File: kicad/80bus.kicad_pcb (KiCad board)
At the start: 2 copper layers, 145 x 130 mm, 70 parts, among them M1 MountingHole_3.2mm_M3_Pad, M2 MountingHole_3.2mm_M3_Pad, M3 MountingHole_3.2mm_M3_Pad, M4 MountingHole_3.2mm_M3_Pad, SW1 SW_SPST, T1 10uF, T2 10uF, U1 4049, U2 TL497_Fixed, U3 LM78L12_TO92, U4 4040, U5 LMC7660

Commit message: Silkscreen tidy
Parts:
- R2: value 680 -> 1K
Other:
- board text added: "6dd64576-4be6-4520-a357-94d72388fa75"
- board text added: "Version 2.3"
- board text removed: "2f09e51e-ebb1-4036-8dc7-cbf1092a799f"
- board text removed: "Version 2.2"
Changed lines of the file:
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@@
   (title_block
     (title "Nascom 2708 / 2716 EPROM programmer")
-    (date "2023-05-21")
-    (rev "2.1")
+    (date "2023-06-21")
+    (rev "2.3")
   )
   (layers
@@
         (effects (font (size 1 1) (thickness 0.15)))
     )
-    (fp_text value "680" (at 15.7734 0.0508) (layer "F.SilkS")
+    (fp_text value "1K" (at 15.7734 0.0508) (layer "F.SilkS")
         (effects (font (size 1 1) (thickness 0.15)))
     )
@@
   (gr_line (start 220.345 77.3176) (end 148.4376 77.3684)
     (stroke (width 0.12) (type default)) (layer "F.SilkS"))
-  (gr_line (start 258.3942 121.4628) (end 258.400852 115.669763)
+  (gr_line (start 257.472446 121.480869) (end 257.470713 115.665387)
     (stroke (width 0.12) (type default)) (layer "F.SilkS"))
   (gr_line (start 220.9038 77.3176) (end 222.150149 77.317978)
     (stroke (width 0.12) (type default)) (layer "F.SilkS"))
-  (gr_line (start 270.8656 109.982) (end 270.8656 85.2932)
+  (gr_line (start 270.8656 109.982) (end 270.863784 86.161088)
     (stroke (width 0.12) (type default)) (layer "F.SilkS"))
-  (gr_line (start 258.400852 115.669763) (end 270.890413 115.669763)
+  (gr_line (start 257.470713 115.665387) (end 270.890413 115.669763)
     (stroke (width 0.12) (type default)) (layer "F.SilkS"))
   (gr_rect (start 171.172735 127.903285) (end 198.043076 157.078709)
@@
     (pts
       (xy 260.898167 126.278685)
-      (xy 258.95907 126.278685)
+      (xy 258.976537 126.278241)
       (xy 258.971586 116.573677)
       (xy 273.867491 116.551824)
@@
   (gr_line (start 214.665167 96.234005) (end 222.150996 96.230094)
     (stroke (width 0.12) (type default)) (layer "F.SilkS"))
-  (gr_line (start 260.9596 85.2932) (end 270.8656 85.2932)
+  (gr_line (start 260.966518 86.161494) (end 270.863784 86.161088)
     (stroke (width 0.12) (type default)) (layer "F.SilkS"))
-  (gr_line (start 215.773 121.4882) (end 258.3942 121.4628)
+  (gr_line (start 217.428511 121.477668) (end 257.472446 121.480869)
     (stroke (width 0.12) (type default)) (layer "F.SilkS"))
   (gr_line (start 148.4376 77.3684) (end 148.4376 105.3592)
@@
   (gr_line (start 217.423733 99.585103) (end 217.428511 121.477668)
     (stroke (width 0.12) (type default)) (layer "F.SilkS"))
-  (gr_line (start 260.9596 77.343) (end 260.9596 85.2932)
+  (gr_line (start 260.9596 77.343) (end 260.966518 86.161494)
     (stroke (width 0.12) (type default)) (layer "F.SilkS"))
   (gr_line (start 214.6554 105.3592) (end 214.665167 96.234005)
@@
     (effects (font (size 1.5 1.5) (thickness 0.3) bold) (justify left bottom))
   )
-  (gr_text "2f09e51e-ebb1-4036-8dc7-cbf1092a799f" (at 214.239431 203.176185) (layer "F.SilkS")
+  (gr_text "6dd64576-4be6-4520-a357-94d72388fa75" (at 214.239431 203.176185) (layer "F.SilkS")
     (effects (font (size 0.8 0.8) (thickness 0.15)))
   )
@@
     (effects (font (size 1.5 1.5) (thickness 0.3) bold) (justify left bottom))
   )
-  (gr_text "Version 2.2" (at 150.954796 201.092783) (layer "F.SilkS")
+  (gr_text "Version 2.3" (at 150.954796 201.092783) (layer "F.SilkS")
     (effects (font (size 1 1) (thickness 0.15)))
   )
@@
   (segment (start 206.751776 132.159351) (end 202.593551 132.159351) (width 0.5) (layer "F.Cu") (net 14))
   (via (at 206.751776 132.159351) (size 0.8) (drill 0.4) (layers "F.Cu" "B.Cu") (net 14))
+  (segment (start 215.586161 110.168839) (end 206.733537 119.021463) (width 0.5) (layer "B.Cu") (net 14))
   (segment (start 217.464 80.4672) (end 217.464 85.3078) (width 1) (layer "B.Cu") (net 14))
   (segment (start 217.5002 85.344) (end 217.5002 91.2368) (width 1) (layer "B.Cu") (net 14))
-  (segment (start 213.995 111.76) (end 206.733537 119.021463) (width 0.5) (layer "B.Cu") (net 14))
+  (segment (start 217.5002 91.2368) (end 215.586161 93.150839) (width 0.5) (layer "B.Cu") (net 14))
   (segment (start 206.733537 132.141112) (end 206.751776 132.159351) (width 0.5) (layer "B.Cu") (net 14))
   (segment (start 206.751776 132.159351) (end 206.733537 132.150232) (width 0.5) (layer "B.Cu") (net 14))
+  (segment (start 215.586161 93.150839) (end 215.586161 110.168839) (width 0.5) (layer "B.Cu") (net 14))
   (segment (start 206.733537 119.021463) (end 206.733537 132.141112) (width 0.5) (layer "B.Cu") (net 14))
-  (segment (start 213.995 94.742) (end 213.995 111.76) (width 0.5) (layer "B.Cu") (net 14))
-  (segment (start 217.5002 91.2368) (end 213.995 94.742) (width 0.5) (layer "B.Cu") (net 14))
   (segment (start 191.5922 174.371) (end 192.5066 175.2854) (width 0.25) (layer "F.Cu") (net 15))
   (segment (start 201.0664 175.2854) (end 202.3872 176.6062) (width 0.25) (layer "F.Cu") (net 15))

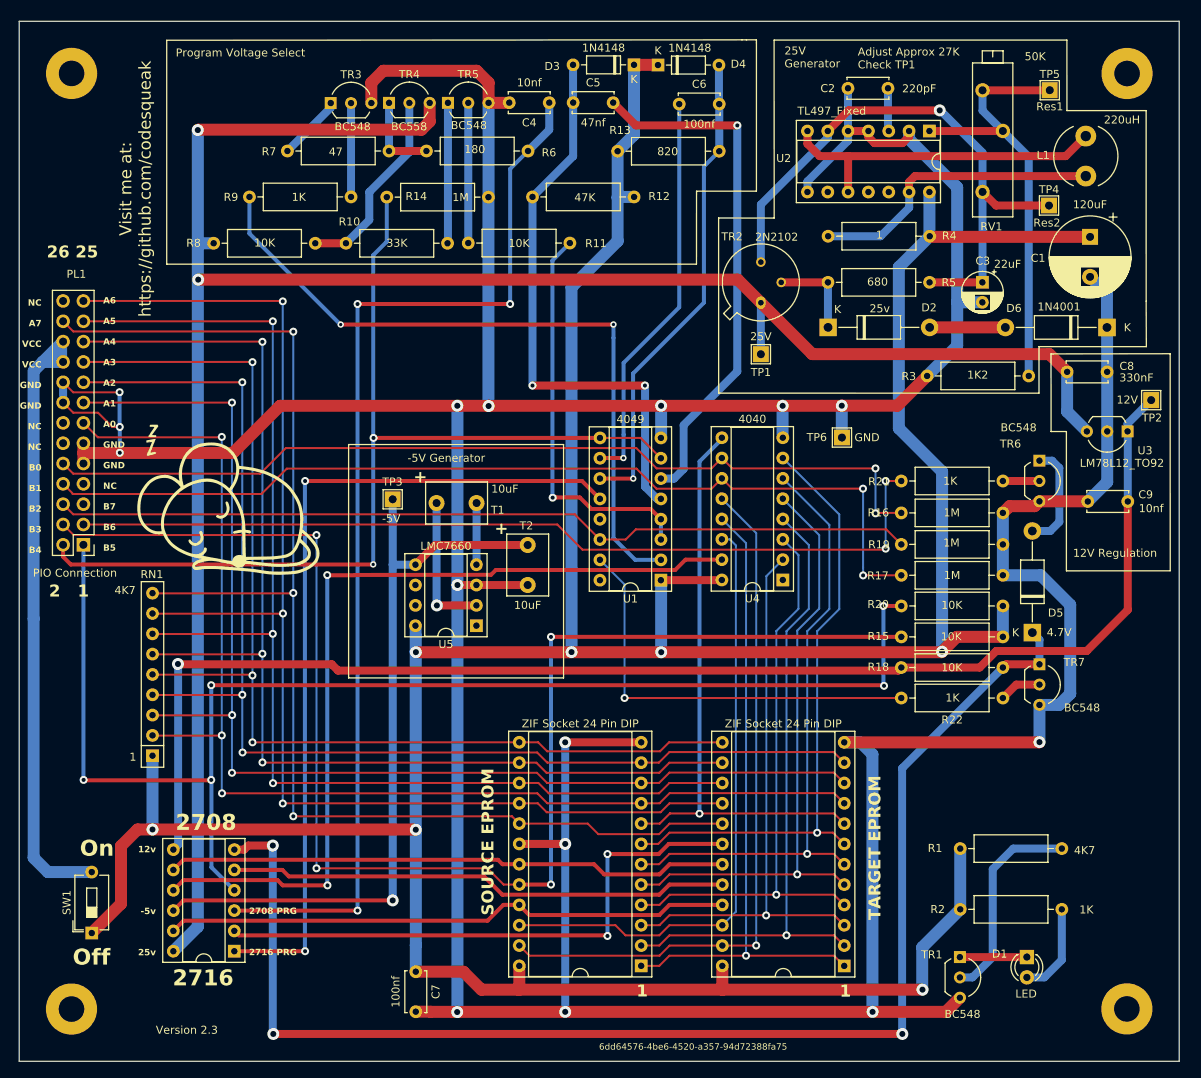
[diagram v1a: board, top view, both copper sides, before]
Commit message: Add aux power feeds
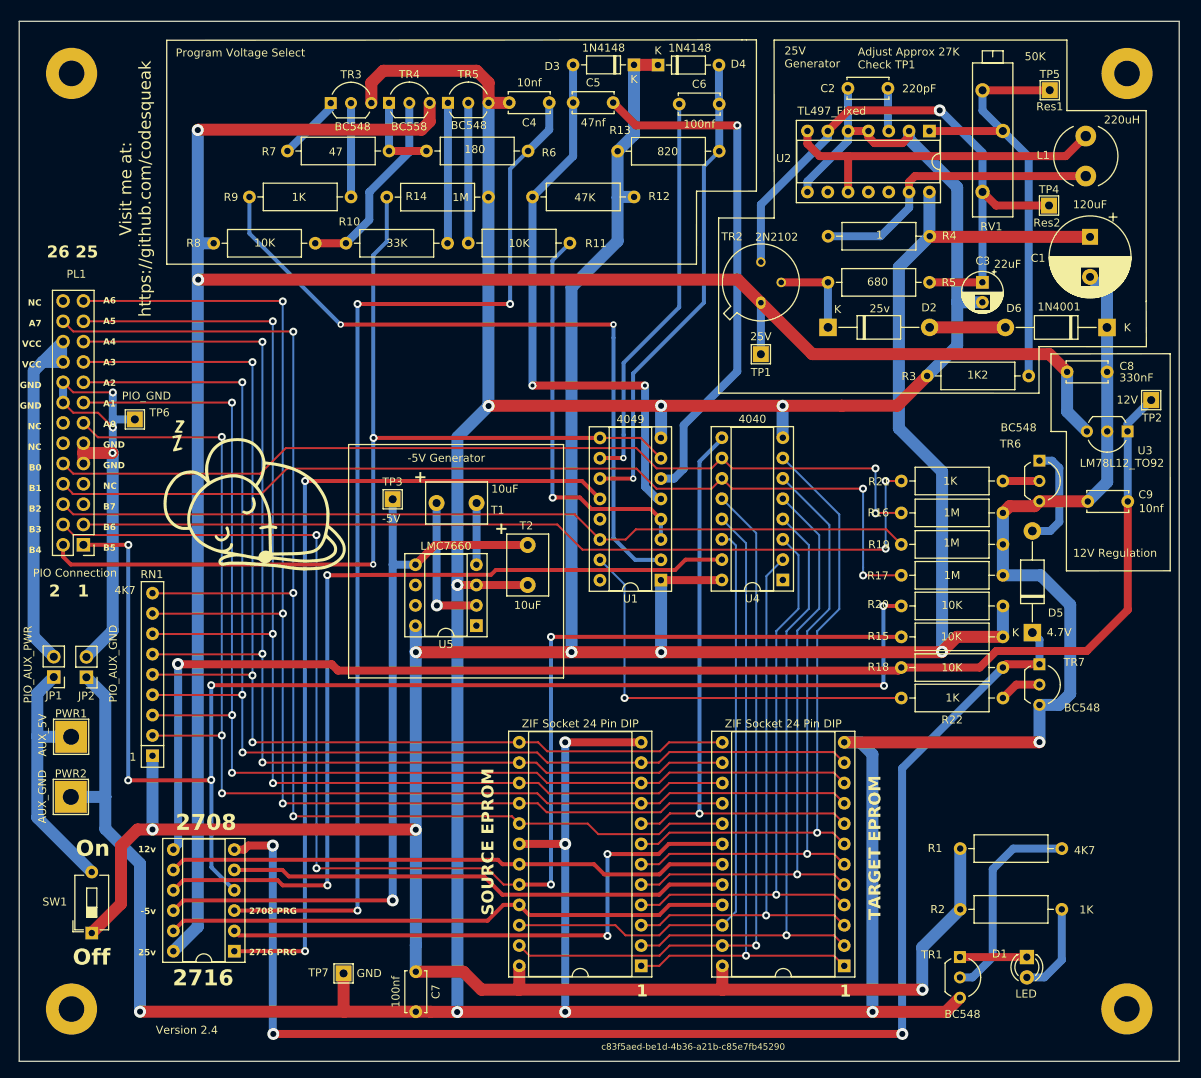
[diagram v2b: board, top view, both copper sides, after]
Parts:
- added JP1: PIO_AUX_PWR, Connector_PinHeader_2.54mm:PinHeader_1x02_P2.54mm_Vertical, F.Cu at (134.3, 157.0)
- added JP2: PIO_AUX_GND, Connector_PinHeader_2.54mm:PinHeader_1x02_P2.54mm_Vertical, F.Cu at (138.4, 157.0)
- added PWR1: AUX_5V, TestPoint:TestPoint_THTPad_4.0x4.0mm_Drill2.0mm, F.Cu at (136.5, 164.4)
- added PWR2: AUX_GND, TestPoint:TestPoint_THTPad_4.0x4.0mm_Drill2.0mm, F.Cu at (136.5, 171.9)
- added TP7: GND, TestPoint:TestPoint_THTPad_2.0x2.0mm_Drill1.0mm, F.Cu at (170.5, 194.0)
- TP6: value GND -> PIO_GND
- moved TP6 88.4 mm to (144.5, 124.8)
- moved G1 3.32 mm to (158.8, 134.9)
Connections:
- PL1 pad 11: GND -> PIO_GND
- PL1 pad 16: GND -> PIO_GND
- PL1 pad 18: GND -> PIO_GND
- PL1 pad 9: GND -> PIO_GND
- SW1 pad 2: VCC -> Net-(JP1-A)
- TP6 pad 1: GND -> PIO_GND
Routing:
- net PIO_GND: track 0.00 -> 60.0 mm, vias 0 -> 3
- net Net-(JP1-A): track 0.00 -> 32.3 mm
- net VCC: track 83.1 -> 51.1 mm
- net GND: track 615.8 -> 620.1 mm, vias 15 -> 11
- net B5: track 168.6 -> 168.7 mm, vias 5 -> 6
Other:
- board text added: "Version 2.4"
- board text added: "c83f5aed-be1d-4b36-a21b-c85e7fb45290"
- board text removed: "6dd64576-4be6-4520-a357-94d72388fa75"
- board text removed: "Version 2.3"

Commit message: Add soft start
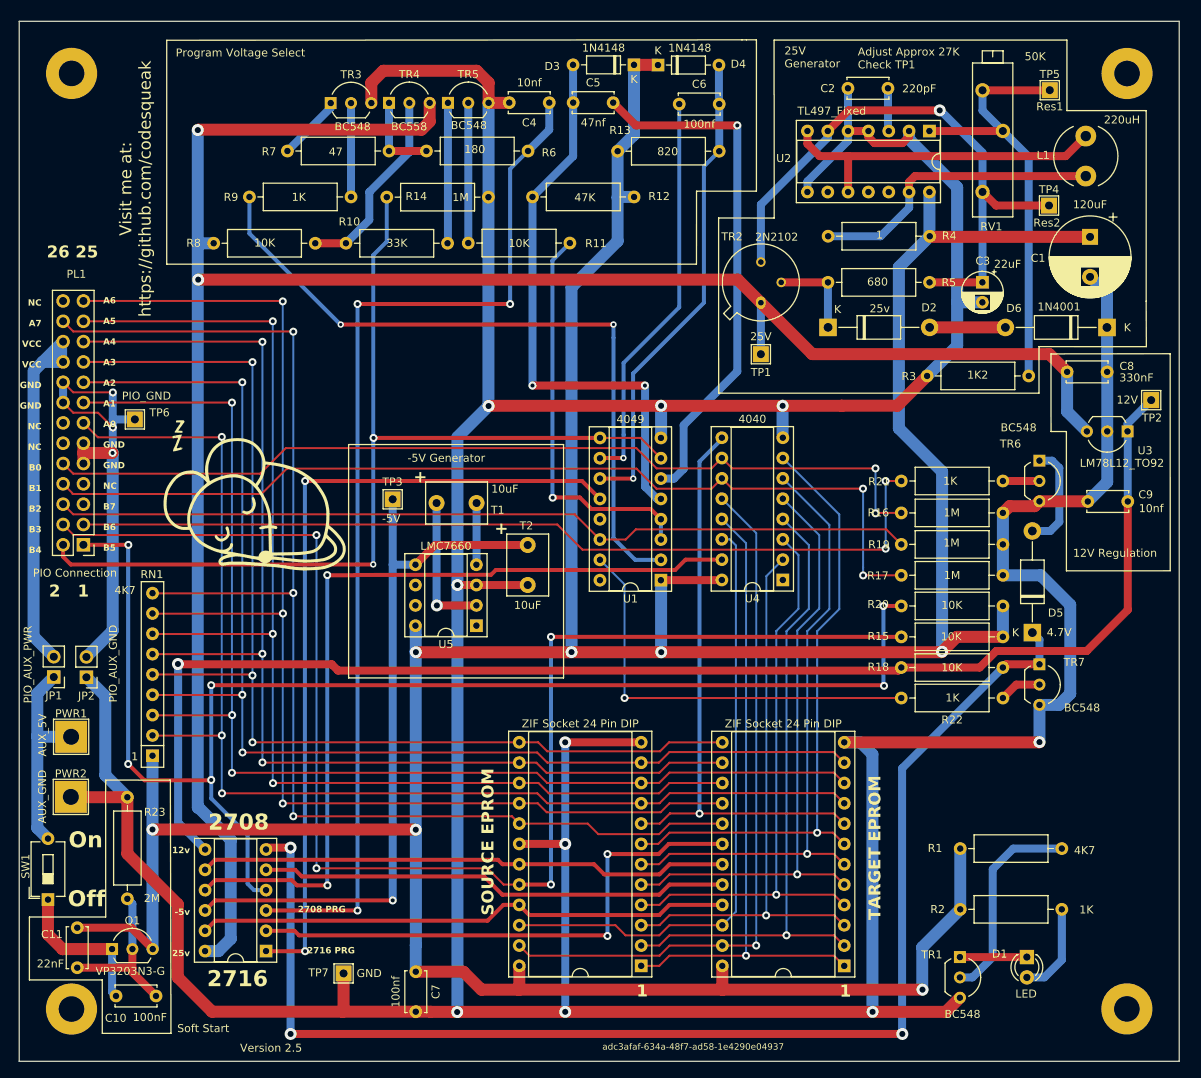
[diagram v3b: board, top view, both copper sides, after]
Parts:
- added C10: 100nF, Capacitor_THT:C_Disc_D5.0mm_W2.5mm_P5.00mm, F.Cu at (142.1, 196.8)
- added C11: 22nF, Capacitor_THT:C_Disc_D5.0mm_W2.5mm_P5.00mm, F.Cu at (137.2, 188.3)
- added Q1: VP3203N3-G, Package_TO_SOT_THT:TO-92L_Inline_Wide, F.Cu at (141.6, 191.0)
- added R23: 2M, Resistor_THT:R_Axial_DIN0309_L9.0mm_D3.2mm_P12.70mm_Horizontal, F.Cu at (143.5, 184.7)
- moved SW1 6.88 mm to (133.6, 184.8)
- moved SW_2708_2716_1 3.97 mm to (160.9, 191.2)
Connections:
- SW1 pad 1: SWITCHED 5V -> Net-(Q1-S)
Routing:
- net Net-(Q1-G): track 0.00 -> 20.6 mm
- net Net-(Q1-S): track 0.00 -> 19.2 mm
- net SWITCHED 5V: track 450.0 -> 458.3 mm
- net Net-(JP1-A): track 32.3 -> 25.9 mm
- net 2716_PRG_PWR: track 105.4 -> 101.4 mm
- net GENERATED -5V: track 96.0 -> 92.0 mm
- net Net-(SKT1-ZIF-Donor_1-Pin_21): track 71.0 -> 67.0 mm
- net Net-(SW_2708_2716_1-Pin_9): track 109.0 -> 105.0 mm
- net Net-(SKT1-ZIF-Donor_1-Pin_19): track 70.4 -> 66.5 mm
- net 2708_PRG_PWR: track 137.5 -> 133.5 mm
- net Net-(SKT2-ZIF-Target_1-Pin_20): track 62.8 -> 58.8 mm
- net Net-(SKT2-ZIF-Target_1-Pin_18): track 72.0 -> 68.0 mm
- net Net-(D5-K): track 166.5 -> 162.6 mm
- net GENERATED 25V: track 265.9 -> 268.7 mm
- net GND: track 620.1 -> 617.6 mm, vias 11 -> 10
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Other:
- board text added: "Soft Start"
- board text added: "Version 2.5"
- board text added: "adc3afaf-634a-48f7-ad58-1e4290e04937"
- board text removed: "Version 2.4"
- board text removed: "c83f5aed-be1d-4b36-a21b-c85e7fb45290"

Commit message: Minor error - wrong resistor value as R13
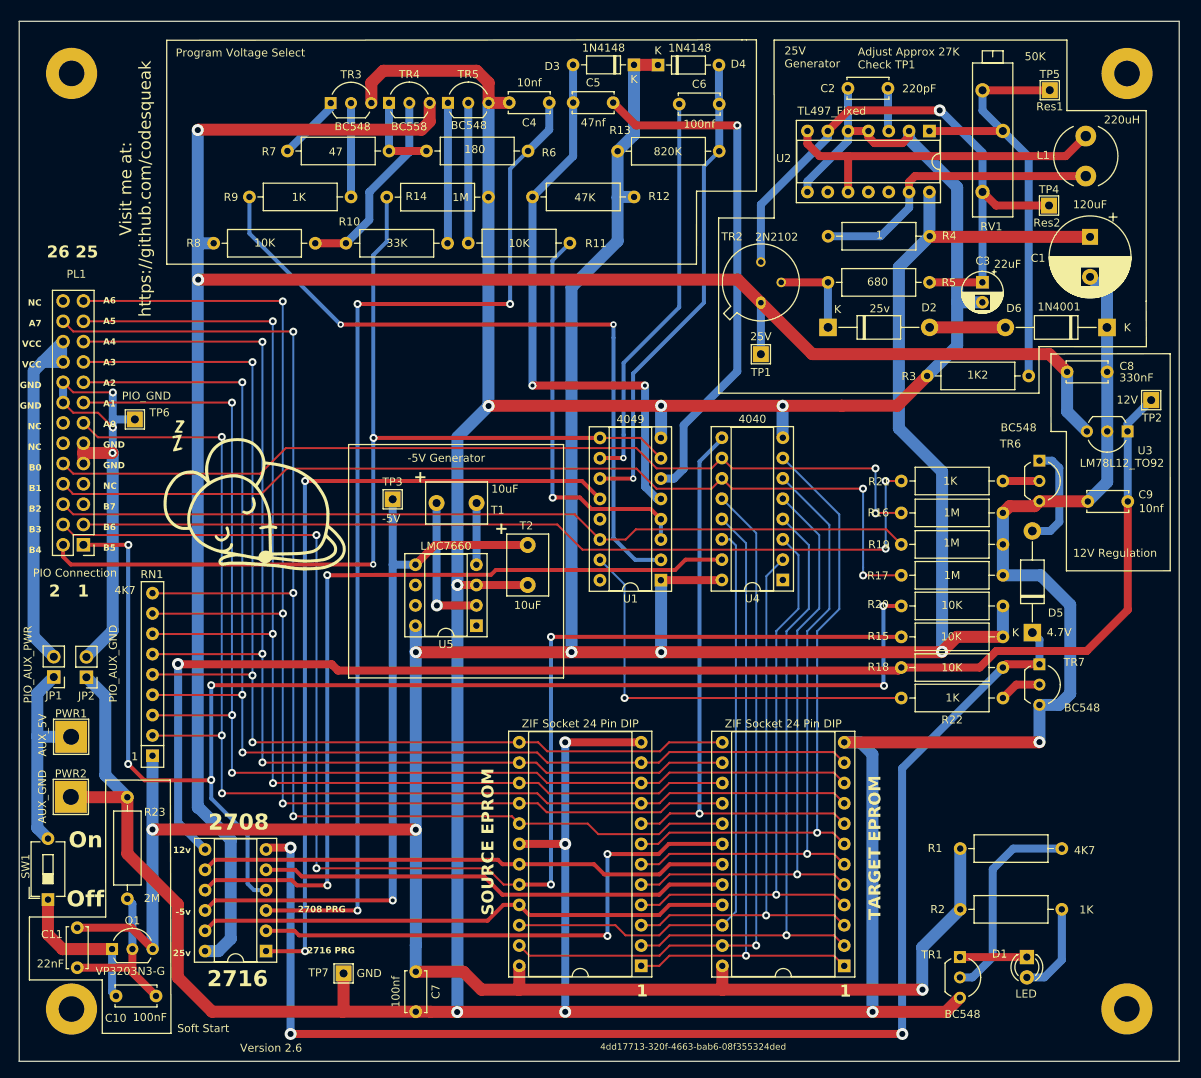
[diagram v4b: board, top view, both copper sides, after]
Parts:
- R13: value 820 -> 820K
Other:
- board text added: "4dd17713-320f-4663-bab6-08f355324ded"
- board text added: "Version 2.6"
- board text removed: "Version 2.5"
- board text removed: "adc3afaf-634a-48f7-ad58-1e4290e04937"
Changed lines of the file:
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@@
   (title_block
     (title "Nascom 2708 / 2716 EPROM programmer")
-    (date "2023-08-14")
-    (rev "2.5")
+    (date "2023-09-01")
+    (rev "2.6")
   )
   (layers
@@
         (effects (font (size 1 1) (thickness 0.15)))
     )
-    (fp_text value "820" (at 6.258372 0.041469) (layer "F.SilkS")
+    (fp_text value "820K" (at 6.258372 0.041469) (layer "F.SilkS")
         (effects (font (size 1 1) (thickness 0.15)))
     )
@@
     (effects (font (size 1.5 1.5) (thickness 0.3) bold) (justify left bottom))
   )
-  (gr_text "adc3afaf-634a-48f7-ad58-1e4290e04937" (at 214.239431 203.176185) (layer "F.SilkS")
+  (gr_text "4dd17713-320f-4663-bab6-08f355324ded" (at 214.239431 203.176185) (layer "F.SilkS")
     (effects (font (size 0.8 0.8) (thickness 0.15)))
   )
@@
     (effects (font (size 1.5 1.5) (thickness 0.3) bold) (justify left bottom))
   )
-  (gr_text "Version 2.5" (at 161.482753 203.335799) (layer "F.SilkS")
+  (gr_text "Version 2.6" (at 161.482753 203.335799) (layer "F.SilkS")
     (effects (font (size 1 1) (thickness 0.15)))
   )
@@
     (effects (font (size 1 1) (thickness 0.15)) (justify left bottom))
   )
-  (gr_text "12v\n\n\n\n\n\n-5v\n\n\n\n25v\n\n" (at 151.347081 193.244902) (layer "F.SilkS")
+  (gr_text "12v\n\n\n\n\n\n-5v\n\n\n\n25v\n\n" (at 151.457273 193.232889) (layer "F.SilkS")
     (effects (font (size 0.8 0.8) (thickness 0.2) bold) (justify right bottom))
   )
@@
     (effects (font (size 2 2) (thickness 0.5) bold) (justify left bottom))
   )
-  (gr_text "Off" (at 136.058612 185.858247) (layer "F.SilkS")
+  (gr_text "Off" (at 135.903224 185.879132) (layer "F.SilkS")
     (effects (font (size 2 2) (thickness 0.5) bold) (justify left bottom))
   )

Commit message: Update docs
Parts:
- removed M1, M2, M3, M4: MountingHole_3.2mm_M3_Pad, MountingHole:MountingHole_3.2mm_M3_Pad
- added G001: LOGO, 80bus:qr-code, B.Cu at (140.8, 88.4)
- D6: footprint Diode_THT:D_DO-41_SOD81_P12.70mm_Horizontal -> Diode_THT:D_DO-41_SOD81_P10.16mm_Horizontal
- Q1: footprint Package_TO_SOT_THT:TO-92L_Inline_Wide -> Package_TO_SOT_THT:TO-92L_Inline
- SW1: value SW_SPST -> SW_SPDT; footprint Button_Switch_THT:SW_DIP_SPSTx01_Slide_6.7x4.1mm_W7.62mm_P2.54mm_LowProfile -> Connector_PinHeader_2.54mm:PinHeader_1x03_P2.54mm_Vertical
- TR1, TR3, TR4, TR5, TR6, TR7, U3: footprint Package_TO_SOT_THT:TO-92_Inline_Wide -> Package_TO_SOT_THT:TO-92_Inline
- moved SW1 6.85 mm to (136.5, 178.6), turned to 0 degrees
- moved TR4 2.69 mm to (178.8, 84.5), turned to 180 degrees
- moved D5 0.90 mm to (257.5, 151.4)
- moved R23 0.66 mm to (142.9, 184.6)
- moved C10 0.51 mm to (141.6, 196.8)
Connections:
- SW1 pad 1: Net-(Q1-S) -> unconnected-(SW1-A-Pad1)
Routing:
- net GND: track 617.6 -> 630.3 mm
- net Net-(JP1-A): track 25.9 -> 32.2 mm
- net GENERATED 25V: track 268.7 -> 264.8 mm
- net Net-(D2-A): track 9.46 -> 12.0 mm
- net Net-(TR5-C): track 17.5 -> 19.9 mm
- net Net-(U2-Comp): track 55.7 -> 57.5 mm
- net Net-(D5-A): track 13.5 -> 11.7 mm
- net Net-(TR3-C): track 8.24 -> 9.81 mm
- net Net-(TR4-C): track 10.7 -> 11.5 mm
- net Net-(Q1-S): track 19.2 -> 19.8 mm
- net Net-(TR3-B): track 11.7 -> 12.3 mm
- net Net-(TR7-B): track 5.27 -> 5.79 mm
- net Net-(TR6-B): track 4.57 -> 5.09 mm
- net Net-(TR5-B): track 17.5 -> 18.1 mm
- net Net-(TR1-B): track 25.9 -> 25.3 mm
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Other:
- board text added: "4eafc235-6eb6-4a2f-9bc3-fe186b3b2c63"
- board text added: "CS-004"
- board text added: "Docs -->"
- board text added: "IN"
- board text added: "NC"
- board text added: "OUT"
- board text added: "Version 2.7"
- board text removed: "4dd17713-320f-4663-bab6-08f355324ded"
- board text removed: "Version 2.6"
